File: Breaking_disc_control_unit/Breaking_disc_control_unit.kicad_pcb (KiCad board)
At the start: 2 copper layers, 61 parts, among them J1 Conn_02x05_Odd_Even, J2 Conn_02x03_Odd_Even, J3 Conn_01x02, J4 Conn_01x04, J5 Conn_01x03, SW1 SW_Push, U1 MKW31Z256VHT4, U2 TLV4964, U3 MMA8452Q, U4 MPL3115A2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

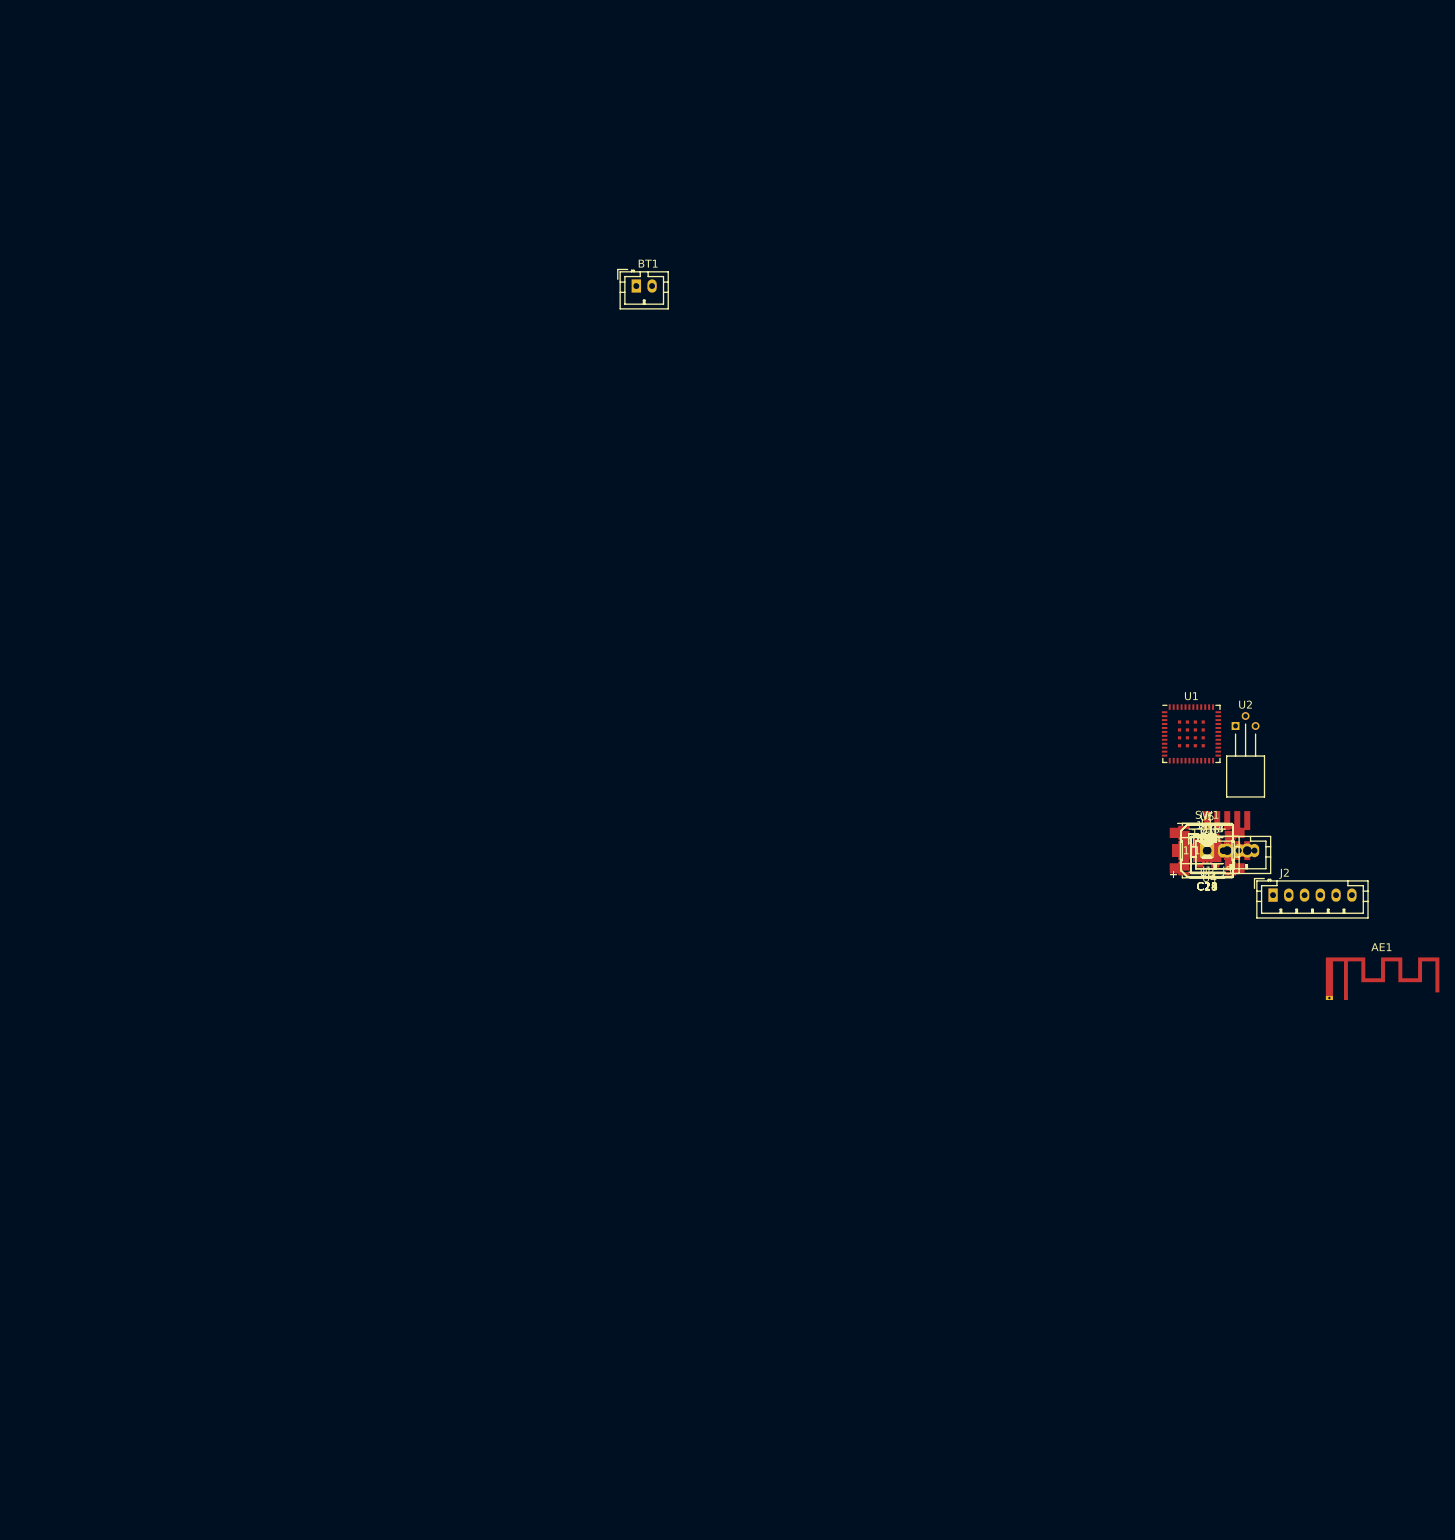
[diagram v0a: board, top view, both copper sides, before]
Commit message: Direction of signal set. Start Layouting
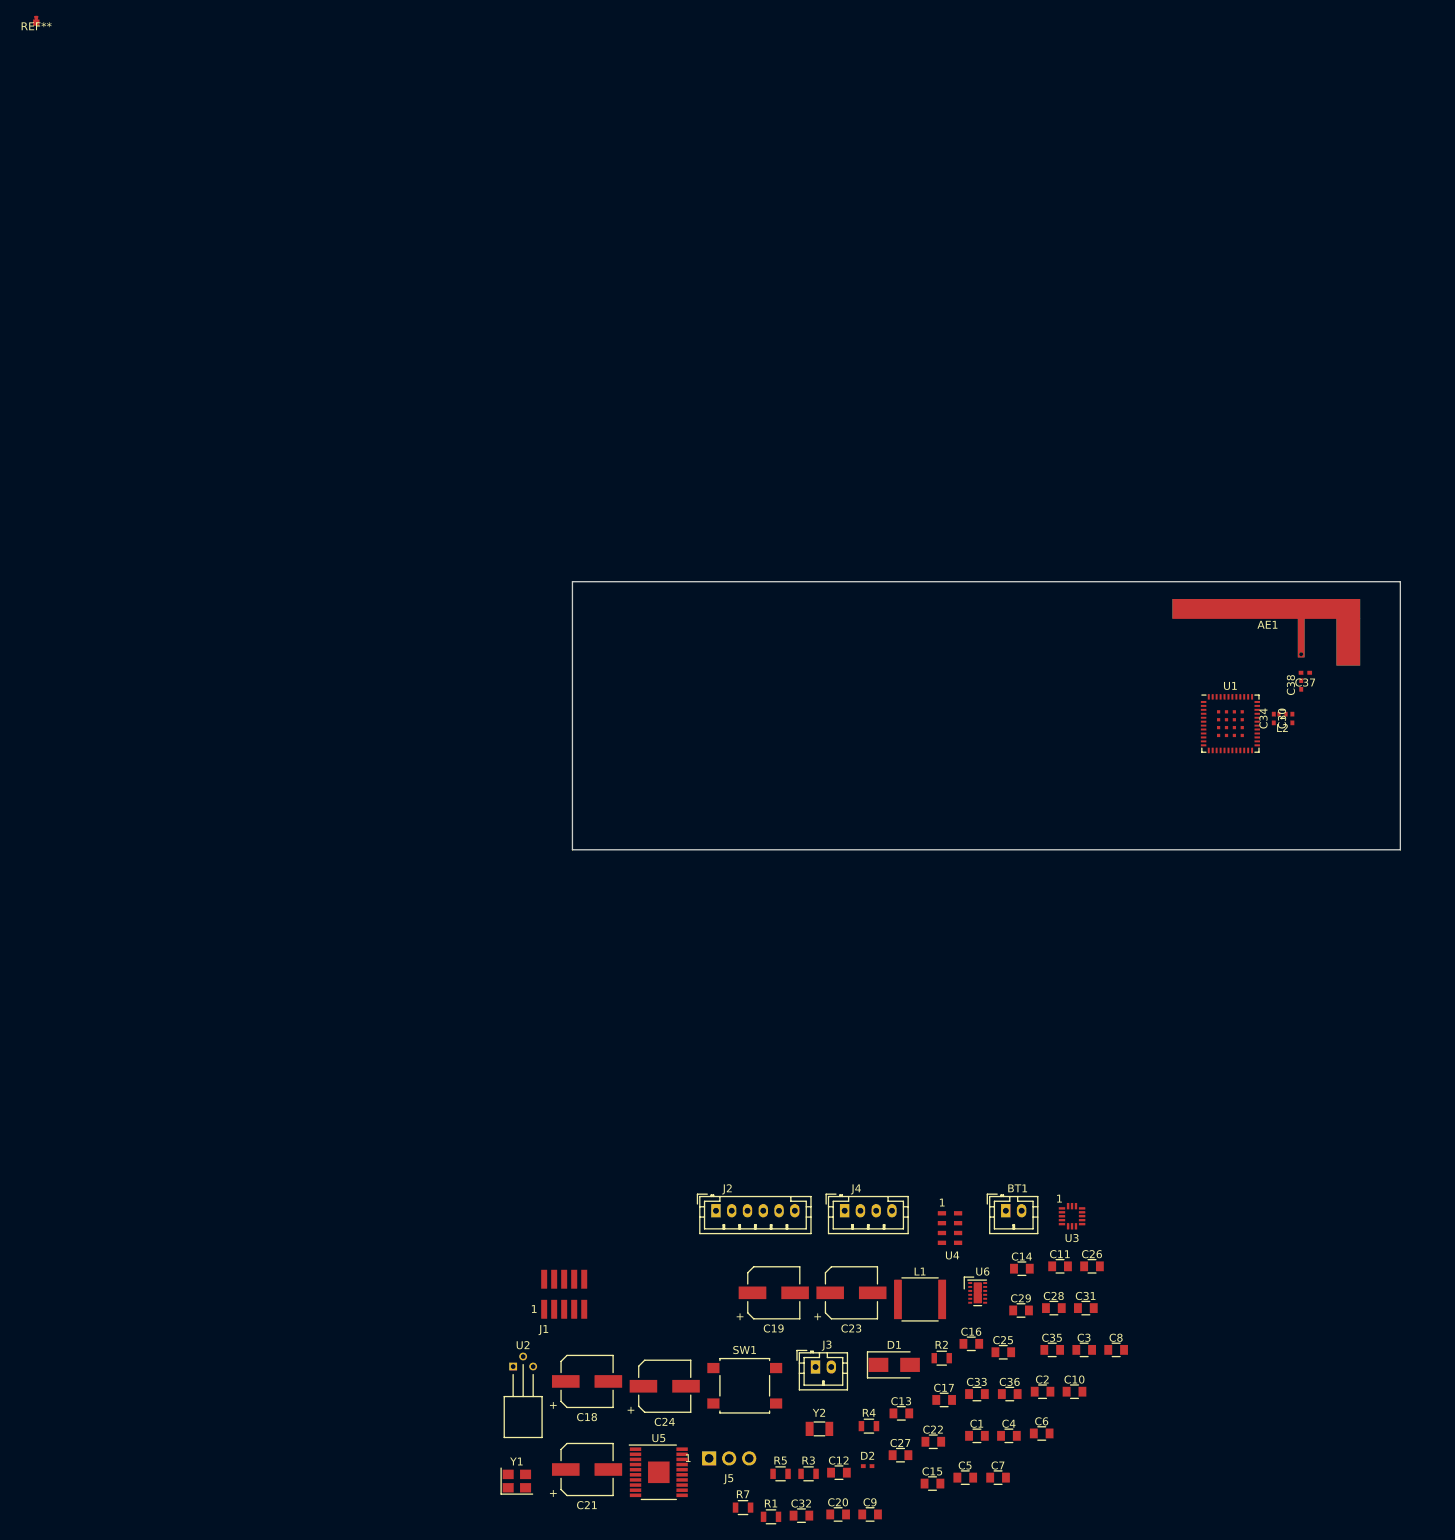
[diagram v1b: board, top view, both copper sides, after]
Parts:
- removed R6: 0, Resistors_SMD:R_0603
- added C35: 10p, Capacitors_SMD:C_0805, F.Cu at (128.8, 168.3)
- added C37: 0.5pF, Capacitors_SMD:C_0402_NoSilk, F.Cu at (160.9, 82.5)
- added C38: 1.5pF, Capacitors_SMD:C_0402_NoSilk, F.Cu at (160.4, 84.0)
- added L2: 5.1nH, Inductors_SMD:L_0402, F.Cu at (158.1, 87.7)
- added REF**: muwave_arcstub, muwave_arcstub, F.Cu at (0.00, 0.00)
- AE1: footprint RF_Antennas:Texas_SWRA117D_2.4GHz_Right -> Footprint_library:IFA
- BT1: value 3.6V Li-Io -> 3.7V LiPo
- C25: value DNP -> 100n
- C30: value 1p2 -> 0.7pF; footprint Capacitors_SMD:C_0603 -> Capacitors_SMD:C_0402_NoSilk
- C34: value DNP -> 0.7pF; footprint Capacitors_SMD:C_0603 -> Capacitors_SMD:C_0402_NoSilk
- C4: value 100n -> 10p
- C6: value 1u -> 10p
- C7: value 10u -> 100n
- R1, R2, R3: value 100k -> 47k
- moved BT1 126.3 mm to (123.0, 150.7)
- moved U2 122.4 mm to (60.5, 170.4)
- moved Y1 118.6 mm to (61.0, 185.0)
- moved C21 111.1 mm to (69.9, 183.5)
- moved U5 105.1 mm to (79.0, 183.8)
- moved C18 103.5 mm to (69.9, 172.3)
- moved J1 102.2 mm to (64.4, 163.2)
- moved R7 102.0 mm to (89.6, 188.3)
- moved R1 101.0 mm to (93.2, 189.5)
- moved J5 99.7 mm to (85.3, 182.1)
- moved C32 98.8 mm to (97.0, 189.3)
- moved C24 96.7 mm to (79.7, 172.9)
- moved C20 96.3 mm to (101.7, 189.2)
- moved R5 95.8 mm to (94.4, 184.0)
- moved C9 94.4 mm to (105.8, 189.2)
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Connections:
- C30 pad 2: Net-(AE1-Pad1) -> Net-(C30-Pad2)
- J2 pad 3: SPI_SOUT_EXT -> SPI1_SOUT_EXT
- J2 pad 4: SPI_PCS0_EXT -> SPI1_PCS0_EXT
- J2 pad 5: SPI_SIN_EXT -> SPI1_SIN_EXT
- J2 pad 6: SPI_SCK_EXT -> SPI1_SCK_EXT
- U1 pad 8: Net-(U1-Pad8) -> GND
- U1 pad 9: Net-(U1-Pad9) -> +3V3
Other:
- board outline added: 105 x 34 mm
- net class Default: clearance 0.2 -> 0.5
- net class RF_trace added: clearance 0.3, trace_width 0.3, via_dia 0.6, via_drill 0.4
- rule pad_to_mask_clearance: 0.2 -> 0
- rule trace_clearance: 0.2 -> 0.5

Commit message: Layout Anordnung
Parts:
- removed AE1: MIFA, Footprint_library:IFA
- added G***: LOGO, Footprint_library:Antenna, F.Cu at (158.6, 76.5)
- Y1: value 32MHz -> Crystal_GND24
- moved REF** 180.3 mm to (161.3, 80.7)
- moved Y1 135.1 mm to (160.6, 93.8), turned to 90 degrees
- moved U2 122.7 mm to (133.8, 72.1), turned to 180 degrees
- moved R1 118.8 mm to (132.1, 77.3), turned to 180 degrees
- moved C32 115.3 mm to (127.9, 78.3), turned to 180 degrees
- moved R7 113.8 mm to (162.6, 101.0), turned to 180 degrees
- moved J5 112.0 mm to (111.9, 73.2)
- moved C5 110.3 mm to (132.8, 75.3), turned to 180 degrees
- moved J1 106.7 mm to (139.3, 87.1), turned to 270 degrees
- moved C21 105.9 mm to (104.3, 83.3), turned to 90 degrees
- moved C27 105.5 mm to (163.5, 91.0), turned to 180 degrees
- moved C12 102.5 mm to (136.7, 87.5), turned to 270 degrees
- moved D2 102.0 mm to (166.0, 101.0), turned to 180 degrees
- moved C4 100.0 mm to (155.8, 84.6), turned to 270 degrees
- moved C6 98.7 mm to (157.5, 84.9), turned to 270 degrees
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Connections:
- J3 pad 1: GND -> VSOURCE
- J3 pad 2: VSOURCE -> GND
- REF** pad 1: (no net) -> Net-(AE1-Pad1)
- Y1 pad 2: XTAL_32MHZ -> GND
- Y1 pad 3: (no net) -> XTAL_32MHZ
- Y1 pad 4: (no net) -> GND
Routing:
- net +3V3: track 0.00 -> 8.79 mm
- net Net-(C17-Pad1): track 0.00 -> 8.53 mm
- net Net-(C30-Pad2): track 0.00 -> 6.38 mm
- net Net-(AE1-Pad1): track 0.00 -> 3.92 mm
- net Net-(C34-Pad2): track 0.00 -> 2.60 mm
- net +BATT: track 0.00 -> 1.30 mm
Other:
- board outline removed
- net class Default: clearance 0.5 -> 0.2
- net class RF_trace_MCU added: clearance 0.2, trace_width 0.3, via_dia 0.6, via_drill 0.4
- rule trace_clearance: 0.5 -> 0.2
- board text added: "Breaking disc control unit V1.0 Robert Näger"
- board text added: "RF trace width? - 0.85 mm (antenna feed width) - recommended from NXP: 1.3 mm but KW31Z pin is smaller"

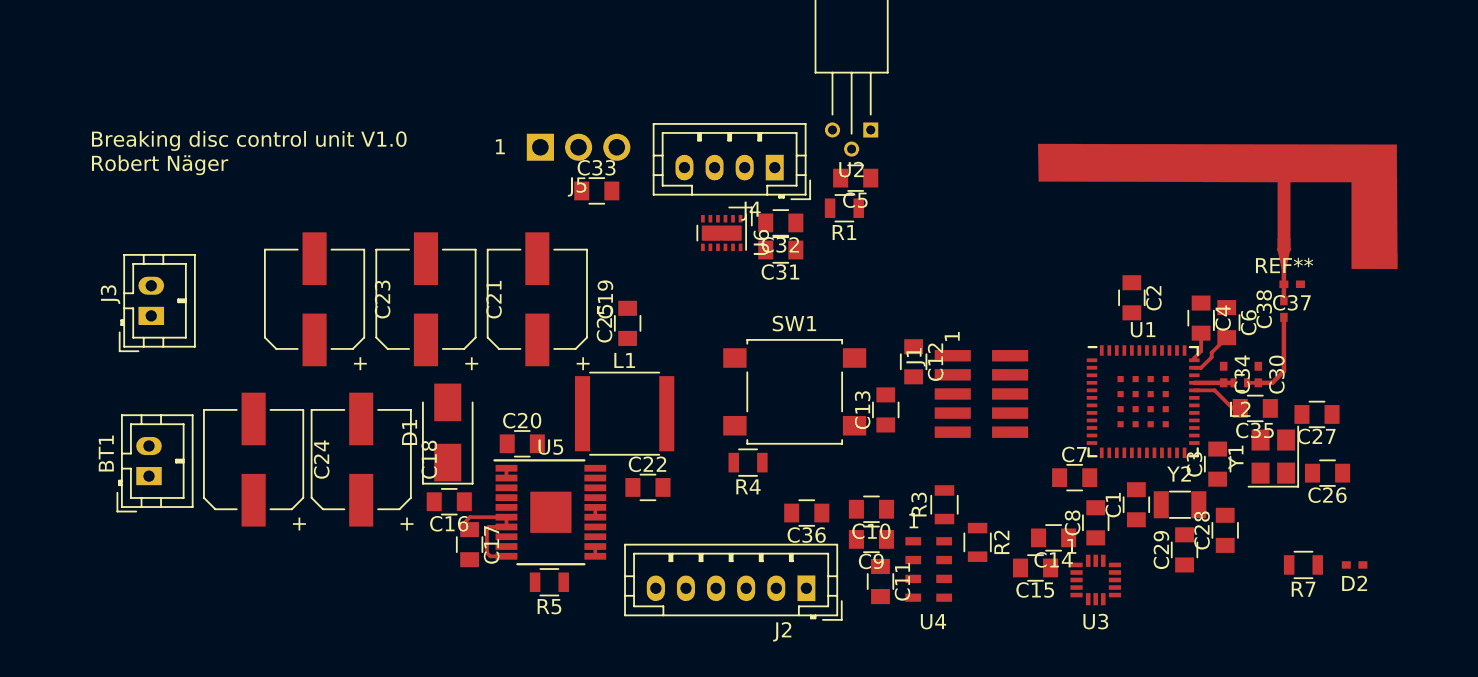
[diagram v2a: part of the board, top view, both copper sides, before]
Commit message: ADC to Battery added -> UV of Battery is disabled because battery directly connected to Actuaturs.
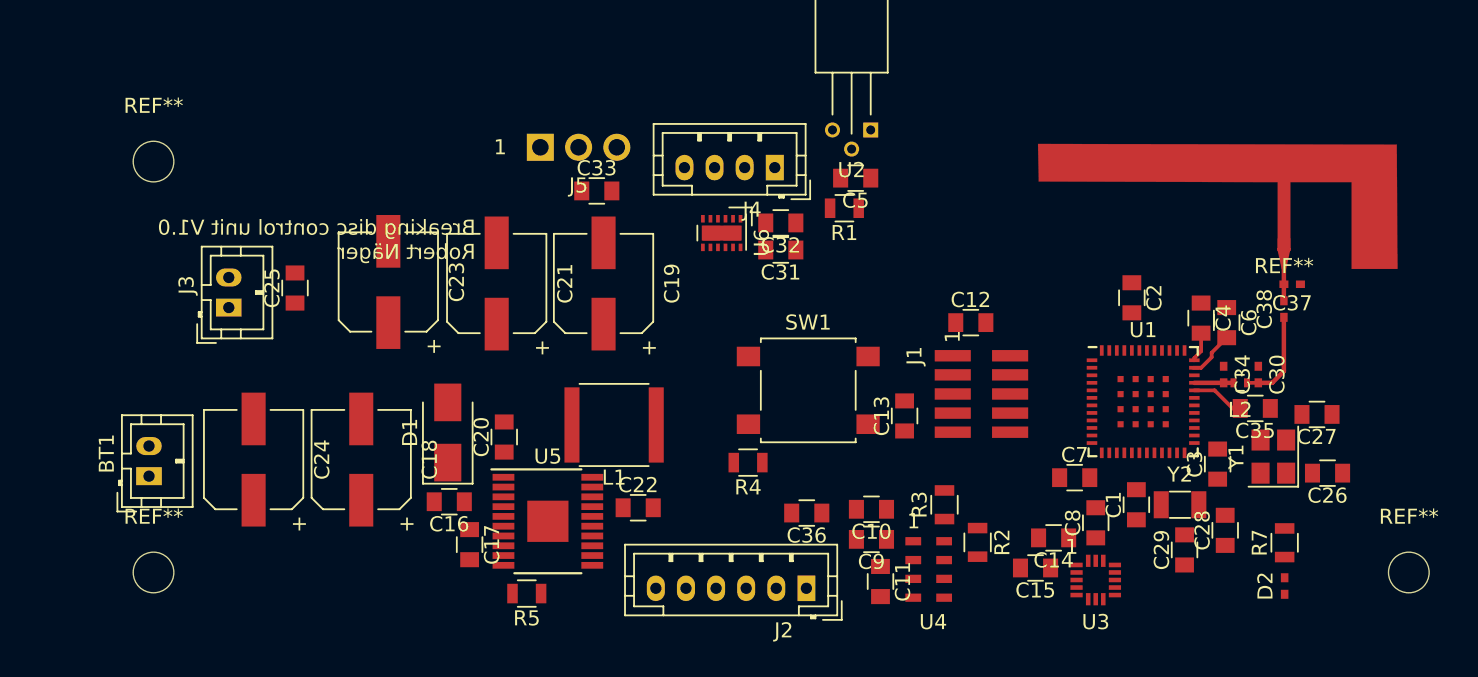
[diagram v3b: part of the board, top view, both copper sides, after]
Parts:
- added REF**: MountingHole_2.7mm_M2.5, Mounting_Holes:MountingHole_2.7mm_M2.5, F.Cu at (169.6, 101.5)
- added REF**: MountingHole_2.7mm_M2.5, Mounting_Holes:MountingHole_2.7mm_M2.5, F.Cu at (86.2, 101.5)
- added REF**: MountingHole_2.7mm_M2.5, Mounting_Holes:MountingHole_2.7mm_M2.5, F.Cu at (86.2, 74.2)
- moved C25 22.2 mm to (95.6, 82.6)
- moved J3 5.18 mm to (91.2, 83.9)
- moved C23 5.03 mm to (101.8, 82.2)
- moved D2 4.86 mm to (161.3, 102.4), turned to 90 degrees
- moved C21 4.82 mm to (109.0, 82.3)
- moved C12 4.60 mm to (140.5, 84.9), turned to 0 degrees
- moved C19 4.52 mm to (116.1, 82.3)
- moved R7 1.93 mm to (161.3, 99.5), turned to 90 degrees
- moved R5 1.68 mm to (111.0, 102.9)
- moved C22 1.50 mm to (118.4, 97.2)
- moved C13 1.31 mm to (136.1, 91.1)
- moved C20 1.28 mm to (109.5, 92.5), turned to 90 degrees
- moved L1 1.03 mm to (116.8, 91.7), turned to 180 degrees
- moved SW1 0.91 mm to (129.7, 89.4)
- moved U5 0.63 mm to (112.4, 98.1)
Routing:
- net Net-(C17-Pad1): track 8.53 -> 0.00 mm
- net +BATT: track 1.30 -> 0.00 mm
